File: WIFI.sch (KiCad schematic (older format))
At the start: 0 parts

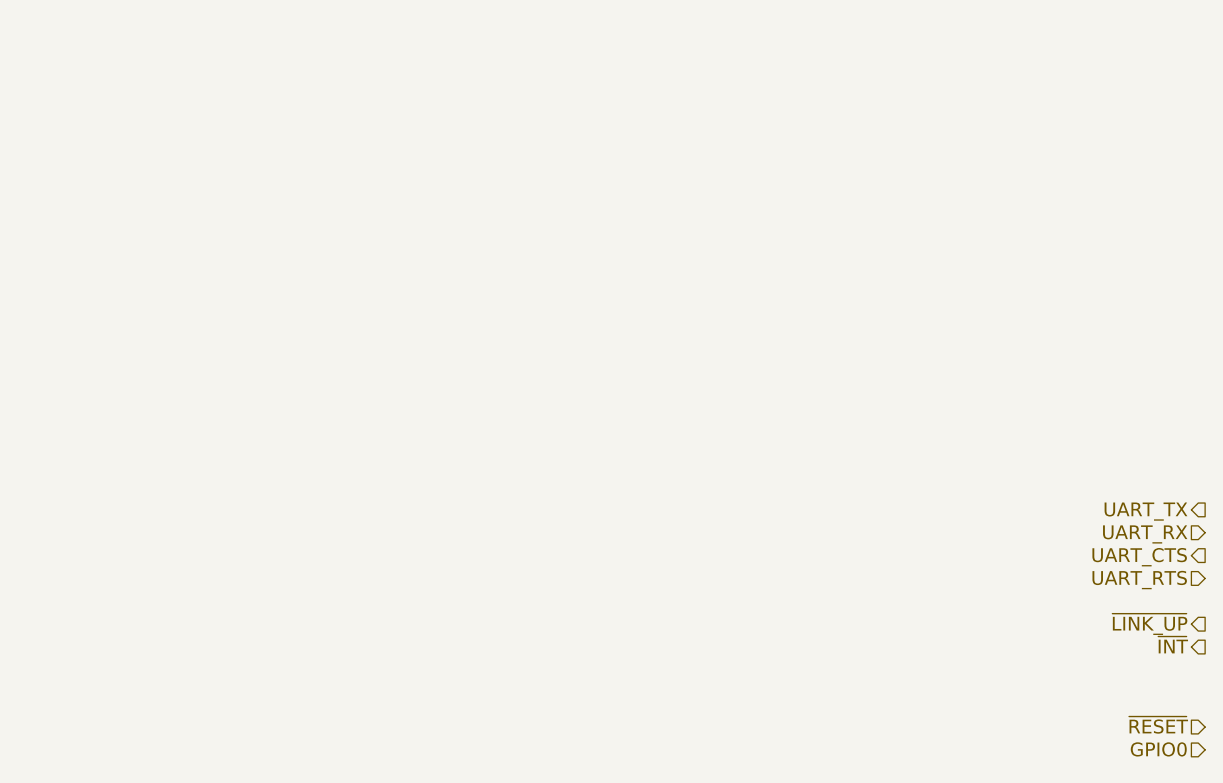
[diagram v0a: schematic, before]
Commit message: current version of the schematics. Audio circuits are still missing.
Audio curcuit topology
Audio from cellphone module is routed to STM
Audio from microphone is routed to STM
STM processes audio and routes microphone data to cellphone module
STM processes audio and routes cellphone audio to amplifier
analog multiplexer can switch route from mic directly to cellphone module and module to speaker
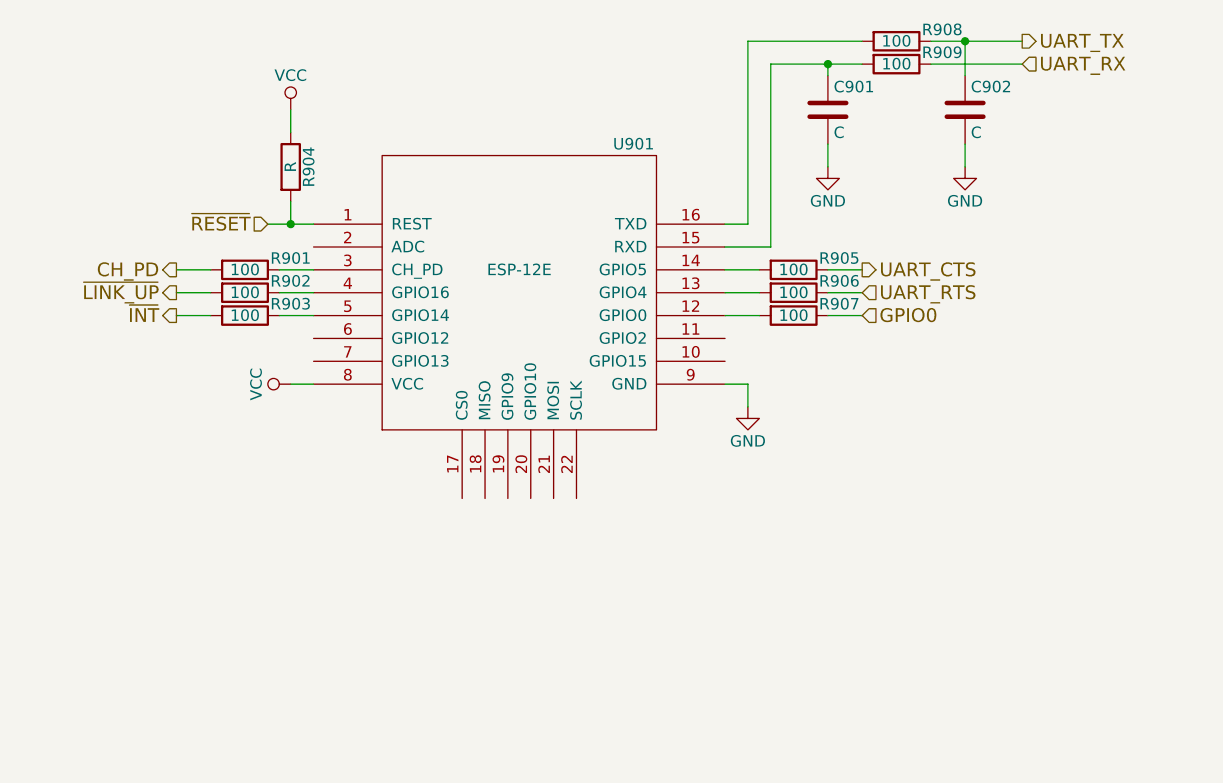
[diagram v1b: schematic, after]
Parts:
- added C901, C902: C, symbol C
- added R901, R902, R903, R905, R906, R907, R908, R909: 100, symbol R
- added R904: R, symbol R
- added U901: ESP-12E, symbol ESP-12E
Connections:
- net GPIO0: now also R907.1
- net UART_CTS: now also R905.1
- net UART_RTS: now also R906.1
- net UART_RX: now also R909.1
- net UART_TX: now also C902.1, R908.1
- net ~INT: now also R903.2
- net ~LINK_UP: now also R902.2
- net ~RESET: now also R904.2, U901.1 (REST)
- new net: R907.2, U901.12 (GPIO0)
- new net: R906.2, U901.13 (GPIO4)
- new net: R905.2, U901.14 (GPIO5)
- new net: C901.1, R909.2, U901.15 (RXD)
- new net: R908.2, U901.16 (TXD)
- new net: R901.1, U901.3 (CH_PD)
- new net: R902.1, U901.4 (GPIO16)
- new net: R903.1, U901.5 (GPIO14)
- new net CH_PD: R901.2
- new net GND: C901.2, C902.2, U901.9 (GND)
- new net VCC: R904.1, U901.8 (VCC)

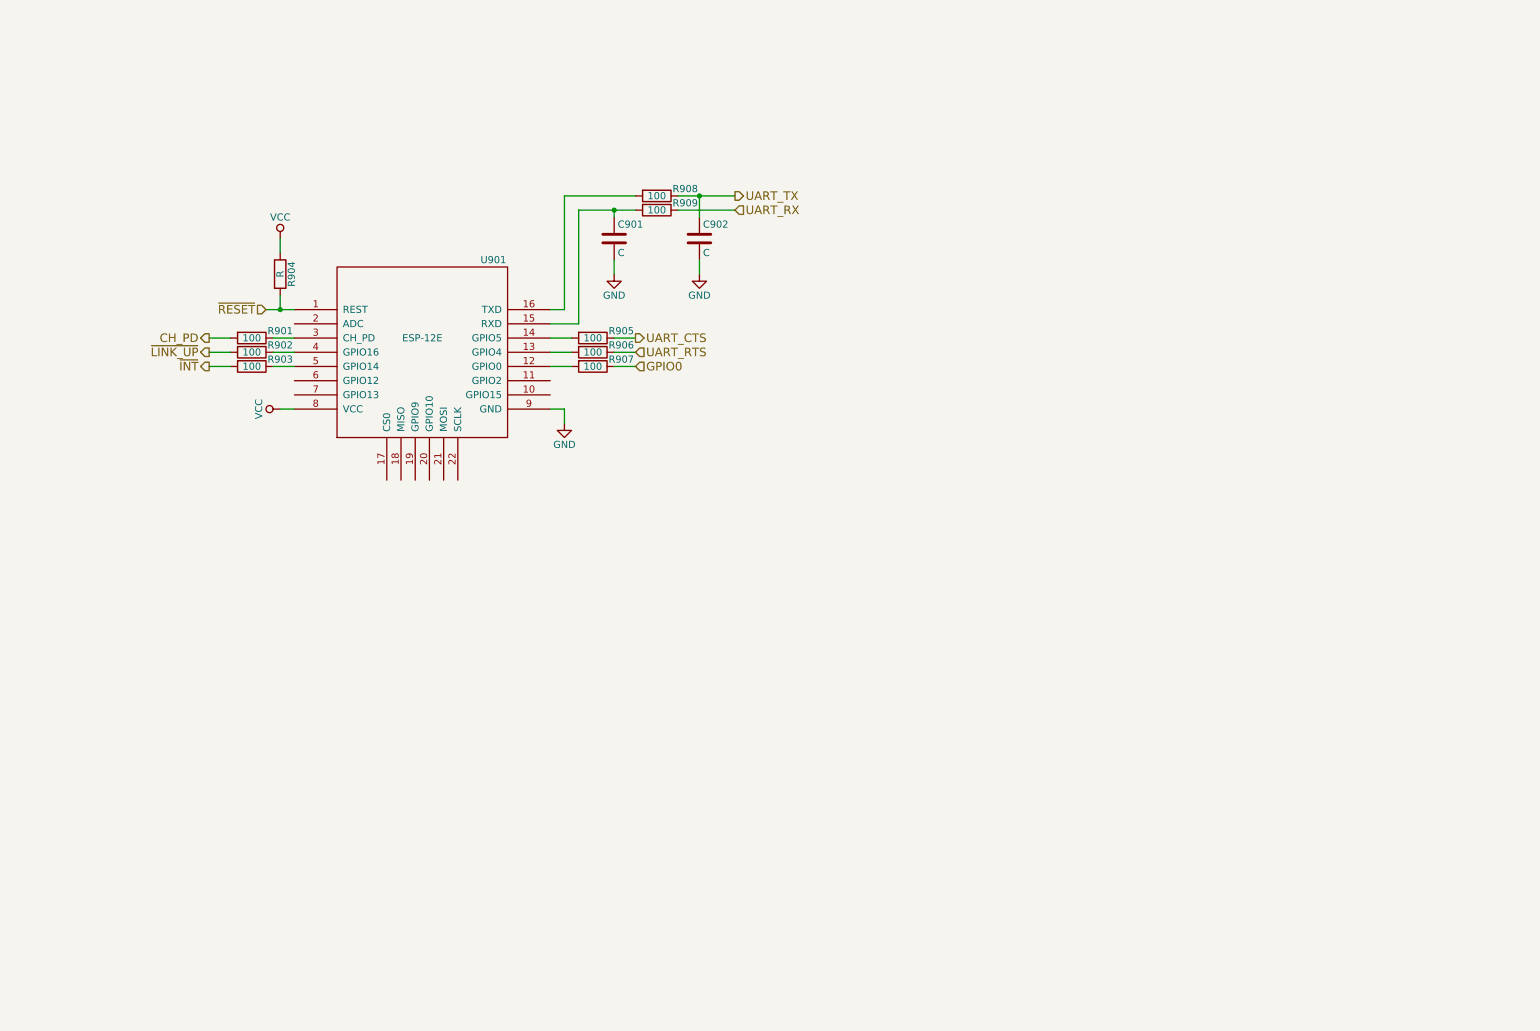
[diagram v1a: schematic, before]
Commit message: added Ti WL1807/1837 Module for WLAN and Bluetooth. added Test Points
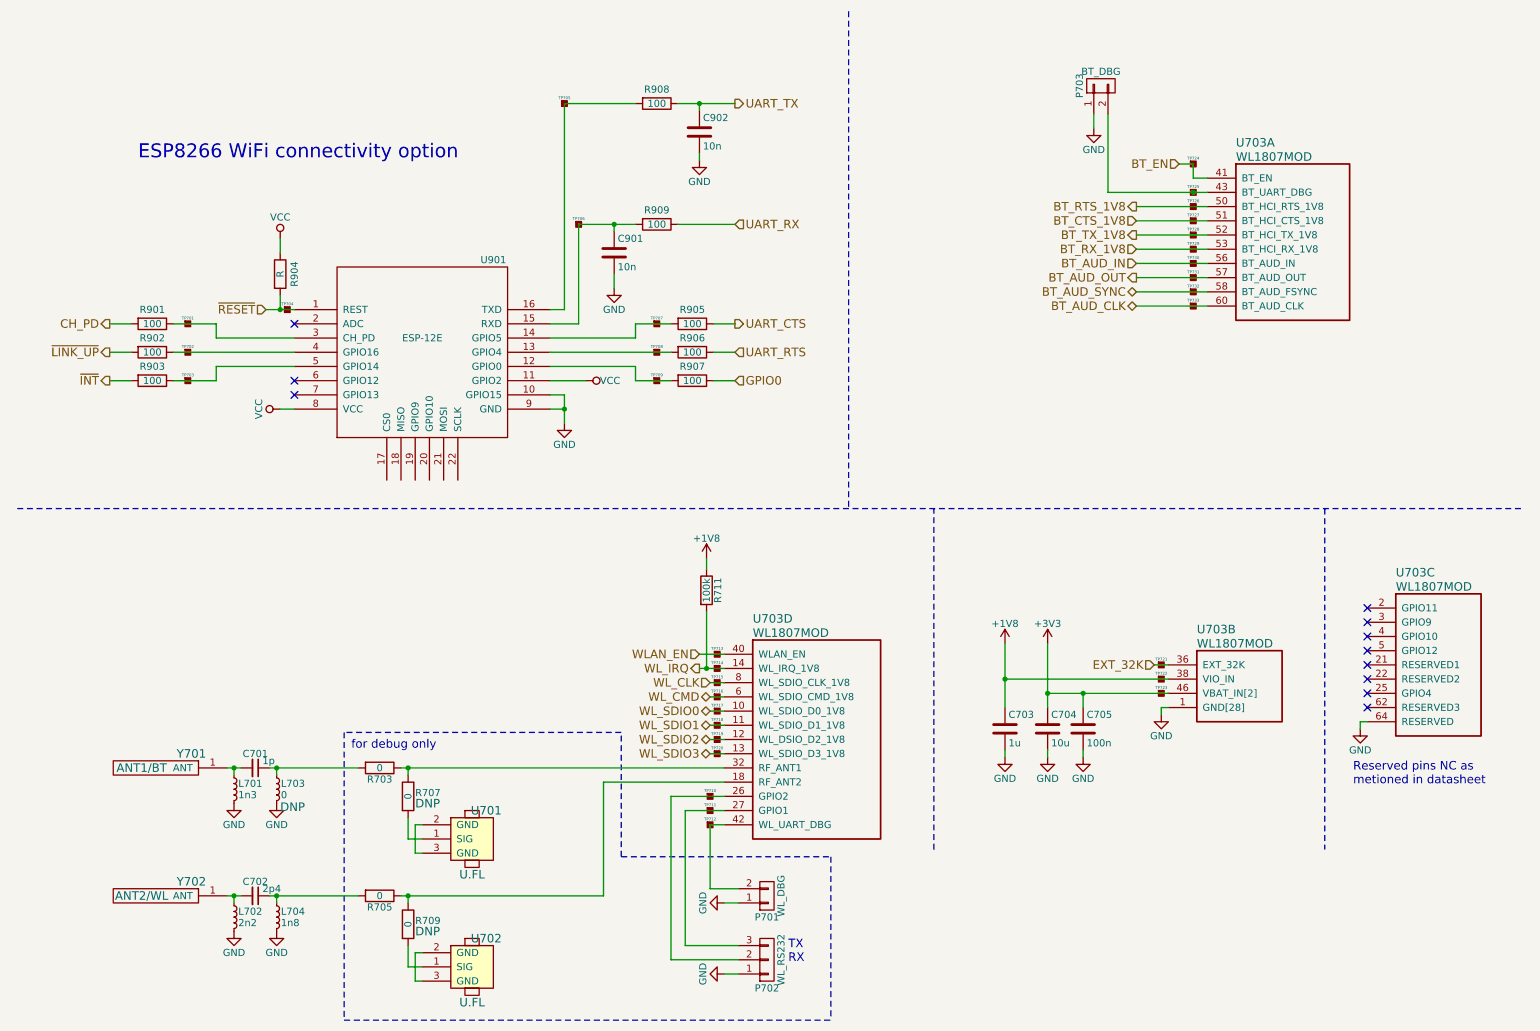
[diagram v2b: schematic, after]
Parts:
- added C701: 1p, symbol C_Small
- added C702: 2p4, symbol C_Small
- added C703: 1u, symbol C
- added C704: 10u, symbol C
- added C705: 100n, symbol C
- added L701: 1n3, symbol L_Small
- added L702: 2n2, symbol L_Small
- added L703: 0, symbol L_Small
- added L704: 1n8, symbol L_Small
- added P701: WL_DBG, symbol CONN_01X02
- added P702: WL_RS232, symbol CONN_01X03
- added P703: BT_DBG, symbol CONN_01X02
- added R703, R705, R707, R709: 0, Resistors_SMD:R_0402, symbol R
- added R711: 100k, symbol R
- added TP701, TP702, TP703, TP704, TP705, TP706, TP707, TP708, TP709, TP710, TP711, TP712, TP713, TP714, TP715, TP716, TP717, TP718, TP719, TP720, TP721, TP722, TP723, TP724, TP725, TP726, TP727, TP728, TP729, TP730, TP731, TP732, TP733: TP, symbol TP
- added U701, U702: U.FL, symbol U.FL
- added U703: WL1807MOD, symbol WL1807MOD
- added Y701: ANT1/BT, symbol W3006
- added Y702: ANT2/WL, symbol W3006
- C901, C902: value C -> 10n
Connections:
- net GND: now also U901.10 (GPIO15), C703.2, C704.2, C705.2, L701.2, L702.2, L703.2, L704.2, P701.1 (P1), P702.1 (P1), P703.1 (P1), U703.1 (GND[28]), U703.15 (GND[28]), U703.16 (GND[28]), U703.17 (GND[28]), U703.19 (GND[28]), U703.20 (GND[28]), U703.23 (GND[28]), U703.24 (GND[28]), U703.28 (GND[28]), U703.29 (GND[28]), U703.30 (GND[28]), U703.31 (GND[28]), U703.33 (GND[28]), U703.34 (GND[28]), U703.35 (GND[28]), U703.37 (GND[28]), U703.39 (GND[28]), U703.44 (GND[28]), U703.45 (GND[28]), U703.48 (GND[28]), U703.49 (GND[28]), U703.54 (GND[28]), U703.55 (GND[28]), U703.59 (GND[28]), U703.61 (GND[28]), U703.63 (GND[28]), U703.64 (RESERVED), U703.7 (GND[28]), U703.9 (GND[28])
- net VCC: now also U901.11 (GPIO2)
- net at C901.1, R909.2, U901.15 (RXD): now also TP706.1
- net at R908.2, U901.16 (TXD): now also TP705.1
- new net: P703.2 (P2), TP725.1, U703.43 (BT_UART_DBG)
- new net: R705.1, R709.1, U703.18 (RF_ANT2)
- new net: P702.2 (P2), U703.26 (GPIO2)
- new net: P702.3 (P3), U703.27 (GPIO1)
- new net: R703.1, R707.1, U703.32 (RF_ANT1)
- new net: P701.2 (P2), TP712.1, U703.42 (WL_UART_DBG)
- new net: C702.2, L702.1, Y702.1 (ANT)
- new net: C701.2, L701.1, Y701.1 (ANT)
- new net: C702.1, L704.1, R705.2
- new net: C701.1, L703.1, R703.2
- new net: R709.2, U702.1 (SIG)
- new net: U702.2 (GND), U702.3 (GND)
- new net: R707.2, U701.1 (SIG)
- new net: U701.2 (GND), U701.3 (GND)
- new net +1V8: C703.1, R711.1, U703.38 (VIO_IN)
- new net +3V3: C704.1, C705.1, U703.46 (VBAT_IN[2]), U703.47 (VBAT_IN[2])
- new net BT_AUD_CLK: U703.60 (BT_AUD_CLK)
- new net BT_AUD_IN: U703.56 (BT_AUD_IN)
- new net BT_AUD_OUT: U703.57 (BT_AUD_OUT)
- new net BT_AUD_SYNC: U703.58 (BT_AUD_FSYNC)
- new net BT_CTS_1V8: U703.51 (BT_HCI_CTS_1V8)
- new net BT_EN: TP724.1, U703.41 (BT_EN)
- new net BT_RTS_1V8: U703.50 (BT_HCI_RTS_1V8)
- new net BT_RX_1V8: U703.53 (BT_HCI_RX_1V8)
- new net BT_TX_1V8: U703.52 (BT_HCI_TX_1V8)
- new net EXT_32K: U703.36 (EXT_32K)
- new net WLAN_EN: U703.40 (WLAN_EN)
- new net WL_CLK: U703.8 (WL_SDIO_CLK_1V8)
- new net WL_CMD: U703.6 (WL_SDIO_CMD_1V8)
- new net WL_IRQ: R711.2, U703.14 (WL_IRQ_1V8)
- new net WL_SDIO0: U703.10 (WL_SDIO_D0_1V8)
- new net WL_SDIO1: U703.11 (WL_SDIO_D1_1V8)
- new net WL_SDIO2: U703.12 (WL_DSIO_D2_1V8)
- new net WL_SDIO3: U703.13 (WL_SDIO_D3_1V8)
- no-connect marks 0 -> 11
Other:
- note added: "ESP8266 WiFi connectivity option"
- note added: "Reserved pins NC as \nmetioned in datasheet"
- note added: "TX\nRX"
- note added: "for debug only"
- moved on the sheet: C901, C902, R901, R902, R903, R905, R906, R907, R908, R909

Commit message: short schematics review and proposed changes
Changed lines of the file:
@@
 $EndComp
 Wire Wire Line
-	4500 2050 4750 2050
-Wire Wire Line
-	4750 2050 4900 2050
+	4500 2050 4900 2050
 $Comp
 L R R908
@@
 	5200 2050 5600 2050
 Wire Wire Line
-	5200 1200 5350 1200
-Wire Wire Line
-	5350 1200 5600 1200
+	5200 1200 5600 1200
 Wire Wire Line
 	4750 2050 4750 2100
@@
 	4500 2750 4300 2750
 Wire Wire Line
-	2300 2650 2400 2650
-Wire Wire Line
-	2400 2650 2500 2650
+	2300 2650 2500 2650
 $Comp
 L R R904
@@
 $EndComp
 Wire Wire Line
-	4400 3250 4400 3350
-Wire Wire Line
-	4400 3350 4400 3450
+	4400 3250 4400 3450
 Wire Wire Line
 	4400 3350 4300 3350
@@
 	8650 5250 7500 5250
 Wire Wire Line
-	7500 5000 7500 5250
-Wire Wire Line
-	7500 5250 7500 5450
-Wire Wire Line
-	7800 5000 7800 5350
-Wire Wire Line
-	7800 5350 7800 5450
+	7500 5000 7500 5450
+Wire Wire Line
+	7800 5000 7800 5450
 Connection ~ 7800 5350
 Wire Wire Line
@@
 $EndComp
 Wire Wire Line
-	7800 5350 8050 5350
-Wire Wire Line
-	8050 5350 8650 5350
+	7800 5350 8650 5350
 $Comp
 L +1V8 #PWR714
@@
 	8825 1625 8825 1725
 Wire Wire Line
-	8225 1825 8825 1825
-Wire Wire Line
-	8825 1825 8925 1825
+	8225 1825 8925 1825
 $Comp
 L TP TP725
@@
 	5425 6725 5625 6725
 Wire Wire Line
-	2025 5875 2075 5875
-Wire Wire Line
-	2075 5875 2125 5875
-Wire Wire Line
-	2025 6775 2075 6775
-Wire Wire Line
-	2075 6775 2125 6775
+	2025 5875 2125 5875
+Wire Wire Line
+	2025 6775 2125 6775
 $Comp
 L L_Small L701
@@
 $EndComp
 Wire Wire Line
-	2325 6775 2375 6775
-Wire Wire Line
-	2375 6775 2950 6775
-Wire Wire Line
-	3250 5875 3300 5875
-Wire Wire Line
-	3300 5875 5525 5875
+	2325 6775 2950 6775
+Wire Wire Line
+	3250 5875 5525 5875
 Wire Wire Line
 	3300 5925 3300 5875
@@
 Connection ~ 3300 6775
 Wire Wire Line
-	3250 6775 3300 6775
-Wire Wire Line
-	3300 6775 4675 6775
-Wire Wire Line
-	2325 5875 2375 5875
-Wire Wire Line
-	2375 5875 2950 5875
+	3250 6775 4675 6775
+Wire Wire Line
+	2325 5875 2950 5875
 $Comp
 L R R707
@@
 	5350 5075 5525 5075
 Wire Wire Line
-	5350 5175 5400 5175
-Wire Wire Line
-	5400 5175 5525 5175
+	5350 5175 5525 5175
 Wire Wire Line
 	5425 5275 5525 5275
